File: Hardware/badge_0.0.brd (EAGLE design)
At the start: 100 x 50 mm, 42 parts, among them CON1 PH_2, IC1 CP2102, SW1 MK12C02, SW2 MK12C02, U4 MCP73832T-2DCI/OT

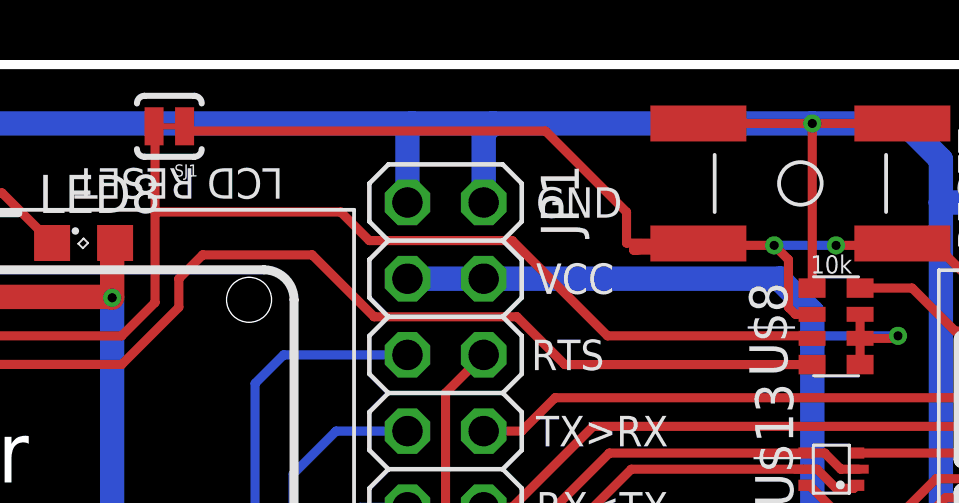
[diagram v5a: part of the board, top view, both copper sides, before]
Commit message: Fixed odd shaped reset trace at reset button
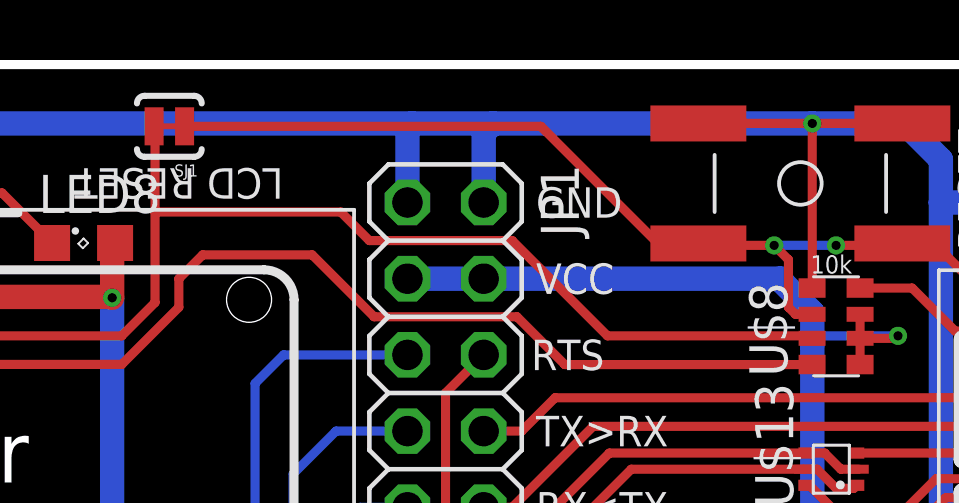
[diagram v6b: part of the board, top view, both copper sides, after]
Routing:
- net RESET: track 61.1 -> 58.0 mm
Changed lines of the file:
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@@
 <?xml version="1.0" encoding="utf-8"?>
 <!DOCTYPE eagle SYSTEM "eagle.dtd">
-<eagle version="7.5.0">
+<eagle version="7.1.0">
 <drawing>
 <settings>
@@
 <wire x1="56.515" y1="41.91" x2="56.515" y2="43.4975" width="0.3048" layer="1"/>
 <wire x1="56.515" y1="43.4975" x2="56.03875" y2="43.97375" width="0.3048" layer="1"/>
-<wire x1="56.03875" y1="43.97375" x2="54.76875" y2="43.97375" width="0.3048" layer="1"/>
 <wire x1="54.76875" y1="43.97375" x2="54.61" y2="43.815" width="0.3048" layer="1"/>
-<wire x1="54.61" y1="43.815" x2="51.353125" y2="43.815" width="0.3048" layer="1"/>
-<wire x1="51.353125" y1="43.815" x2="53.511875" y2="44.0375" width="0.3048" layer="1"/>
-<wire x1="48.41875" y1="47.78375" x2="51.1175" y2="45.085" width="0.3048" layer="1"/>
-<wire x1="51.1175" y1="45.085" x2="51.1175" y2="44.050625" width="0.3048" layer="1"/>
-<wire x1="51.1175" y1="44.050625" x2="53.511875" y2="44.0375" width="0.3048" layer="1"/>
-<wire x1="48.41875" y1="47.78375" x2="36.3855" y2="47.78375" width="0.3048" layer="1"/>
-<wire x1="36.3855" y1="47.78375" x2="36.3855" y2="47.9425" width="0.3048" layer="1"/>
+<wire x1="48.26" y1="47.9425" x2="52.22875" y2="43.97375" width="0.3048" layer="1"/>
+<wire x1="48.26" y1="47.9425" x2="36.3855" y2="47.9425" width="0.3048" layer="1"/>
 <via x="58.1025" y="43.97375" extent="1-16" drill="0.3048" shape="octagon"/>
 <wire x1="58.1025" y1="43.97375" x2="56.03875" y2="43.97375" width="0.3048" layer="16"/>
 <via x="56.03875" y="43.97375" extent="1-16" drill="0.3048" shape="octagon"/>
+<wire x1="56.03875" y1="43.97375" x2="53.511875" y2="43.97375" width="0.3048" layer="1"/>
+<wire x1="53.511875" y1="43.97375" x2="53.511875" y2="44.0375" width="0.3048" layer="1"/>
+<wire x1="52.22875" y1="43.97375" x2="53.0225" y2="43.97375" width="0.3048" layer="1"/>
+<wire x1="53.0225" y1="43.97375" x2="53.448125" y2="43.97375" width="0.3048" layer="1"/>
+<wire x1="53.448125" y1="43.97375" x2="53.511875" y2="44.0375" width="0.3048" layer="1"/>
+<wire x1="54.61" y1="43.815" x2="53.18125" y2="43.815" width="0.3048" layer="1"/>
+<wire x1="53.18125" y1="43.815" x2="53.0225" y2="43.97375" width="0.3048" layer="1"/>
 </signal>
 <signal name="ADC">

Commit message: Minimal nonessential changes
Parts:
- SJ1: value SOLDERJUMPERTRACE -> LCD_RESET
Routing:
- net RX: track 46.7 -> 39.7 mm, vias 0 -> 2
- net TX: track 34.9 -> 38.4 mm
- net VCC: track 267.4 -> 266.9 mm
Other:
- board text added: "PEMH9"

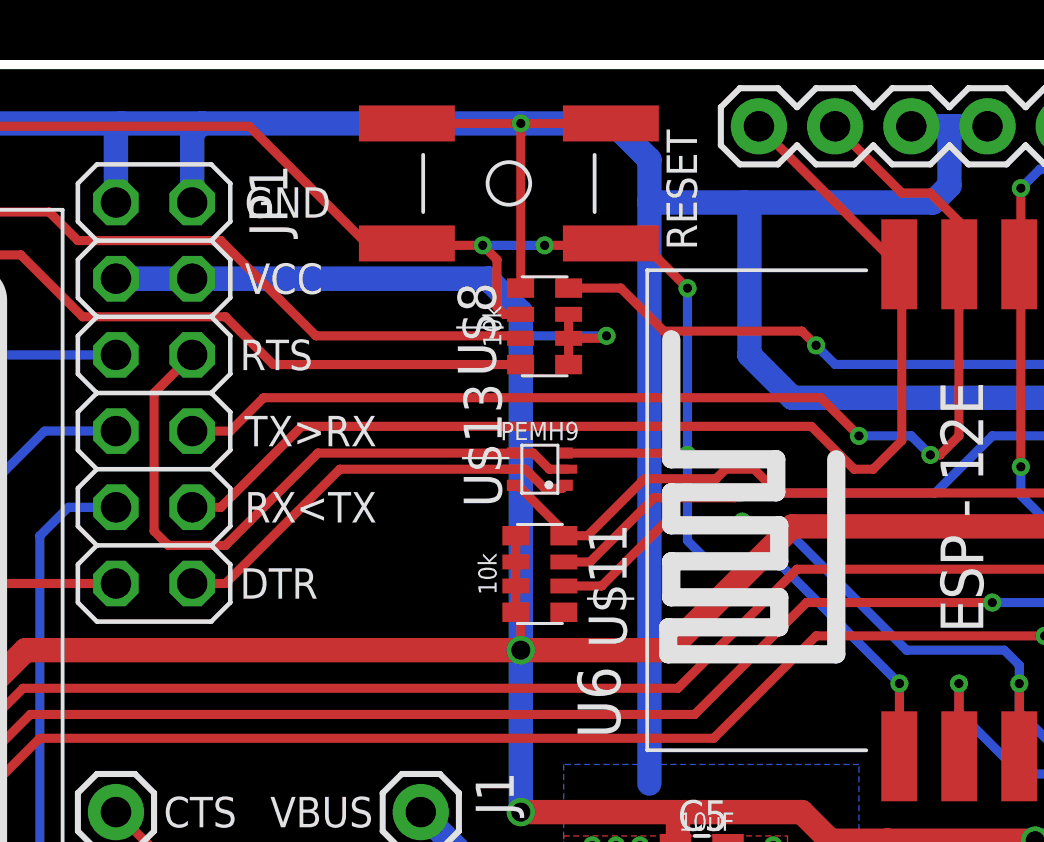
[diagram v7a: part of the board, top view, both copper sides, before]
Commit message: moved res array U to away from RESET button
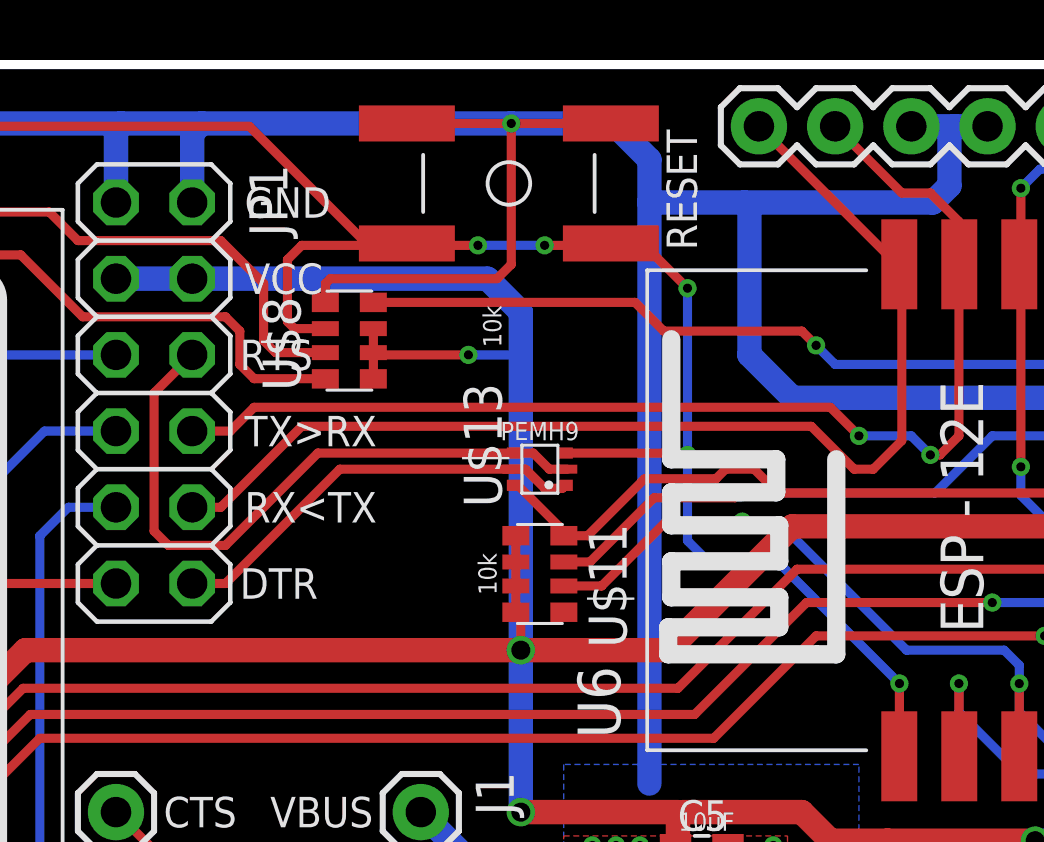
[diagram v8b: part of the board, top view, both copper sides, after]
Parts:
- moved U$8 6.53 mm to (51.6, 40.8)
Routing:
- net GPIO15/SPI_CS: track 140.5 -> 146.8 mm
- net GND: track 388.7 -> 394.9 mm
- net N$3: track 66.7 -> 61.0 mm
- net LCD_RESET: track 76.5 -> 71.3 mm
- net RESET: track 58.0 -> 61.1 mm
- net VCC: track 266.9 -> 267.4 mm
